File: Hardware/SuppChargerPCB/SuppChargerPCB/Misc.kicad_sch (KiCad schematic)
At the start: 11 parts, among them J3 Conn_01x02_Pin, J4 Conn_01x02_Pin, J5 Conn_01x02_Pin, J6 Conn_01x02_Pin, J7 Conn_01x02_Pin, J8 Conn_01x02_Pin

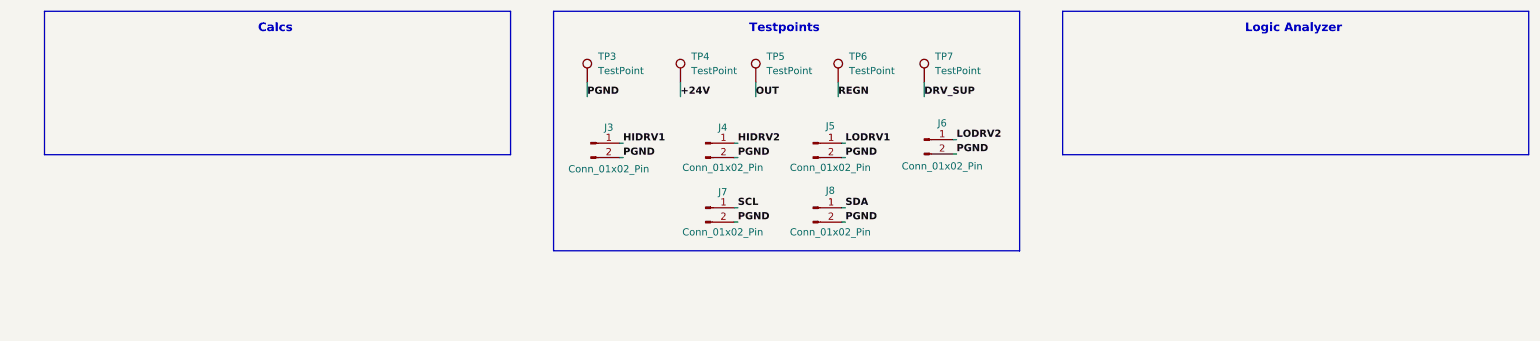
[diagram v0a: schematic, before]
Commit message: added calcs, logic analyzer
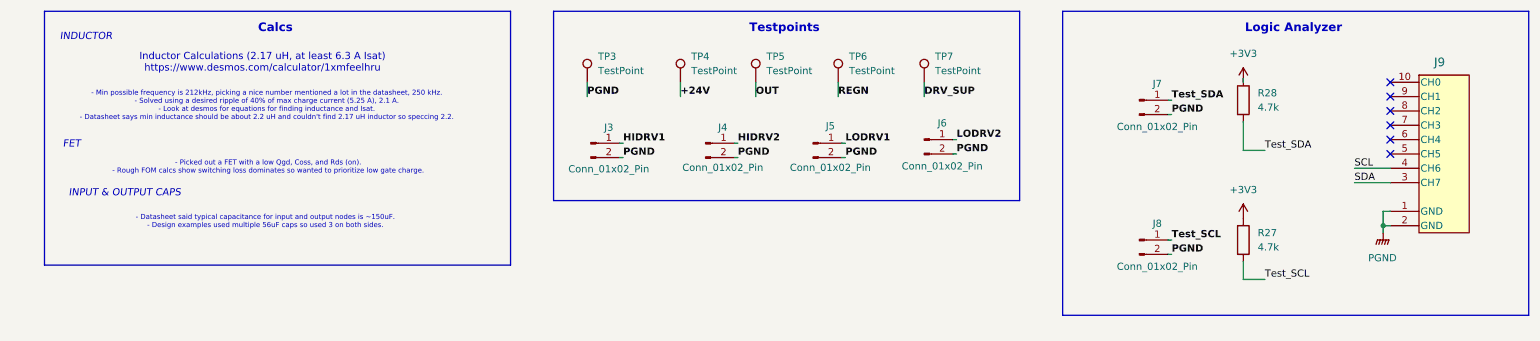
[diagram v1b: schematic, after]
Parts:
- added J9: SFH11-PBPC-D05-ST-BK, UTSVT_Connectors:CONN_SFH11-xxxC-D05-ST-XX_SUL, symbol utsvt_connectors:SFH11-PBPC-D05-ST-BK
- added R27, R28: 4.7k, symbol Device:R
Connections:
- net PGND: now also J9.1 (GND), J9.2 (GND)
- net SCL: now also J9.4 (CH6); no longer J7.1 (Pin_1)
- net SDA: now also J9.3 (CH7); no longer J8.1 (Pin_1)
- new net +3V3: R27.1, R28.1
- new net Test_SCL: J8.1 (Pin_1), R27.2
- new net Test_SDA: J7.1 (Pin_1), R28.2
- no-connect marks 0 -> 6
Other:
- note added: "- Datasheet said typical capacitance for input and output nodes is ~150uF. - Design examples used multiple 56uF caps so used 3 on both sides."
- note added: "- Min possible frequency is 212kHz, picking a nice number mentioned a lot in the datasheet, 250 kHz. - Solved using a desired ripple of 40% of max charge current (5.25 A), 2.1 A. - Look at desmos for equations for finding inductance and Isat. - Datasheet says min inductance should be about 2.2 uH and couldn't find 2.17 uH inductor so speccing 2.2."
- note added: "- Picked out a FET with a low Qgd, Coss, and Rds (on). - Rough FOM calcs show switching loss dominates so wanted to prioritize low gate charge."
- note added: "FET"
- note added: "INDUCTOR"
- note added: "INPUT & OUTPUT CAPS"
- note added: "Inductor Calculations (2.17 uH, at least 6.3 A Isat) https://www.desmos.com/calculator/1xmfeelhru"

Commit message: need to assign bulk cap
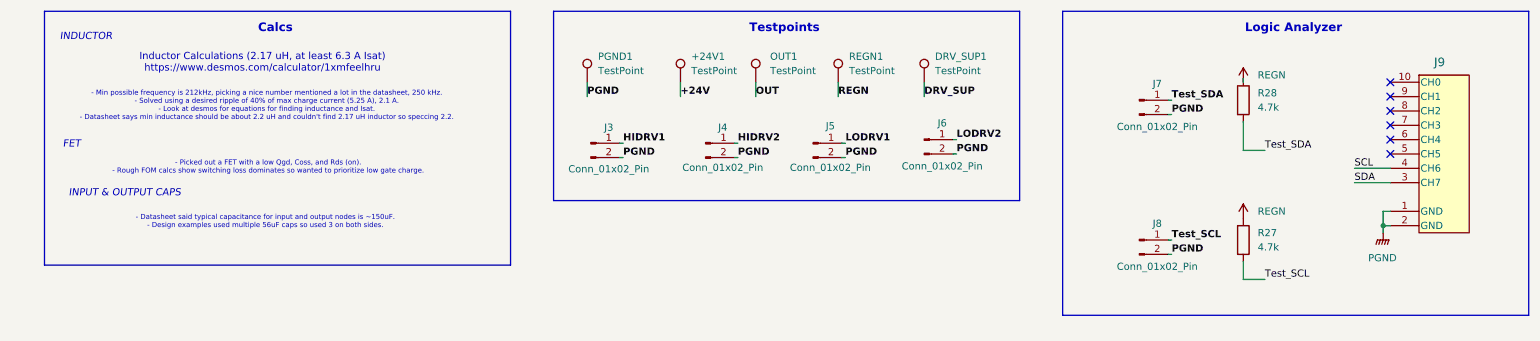
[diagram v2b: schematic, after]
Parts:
- +24V1: renamed from TP4; footprint (none) -> Connector_PinHeader_2.54mm:PinHeader_1x01_P2.54mm_Vertical
- DRV_SUP1: renamed from TP7; footprint (none) -> Connector_PinHeader_2.54mm:PinHeader_1x01_P2.54mm_Vertical
- J3, J4, J5, J6, J7, J8: footprint (none) -> Connector_PinHeader_2.54mm:PinHeader_1x02_P2.54mm_Vertical
- OUT1: renamed from TP5; footprint (none) -> Connector_PinHeader_2.54mm:PinHeader_1x01_P2.54mm_Vertical
- PGND1: renamed from TP3; footprint (none) -> Connector_PinHeader_2.54mm:PinHeader_1x01_P2.54mm_Vertical
- R27, R28: footprint (none) -> Resistor_SMD:R_0603_1608Metric; P/N (none) -> CRCW06034K70FKEA
- REGN1: renamed from TP6; footprint (none) -> Connector_PinHeader_2.54mm:PinHeader_1x01_P2.54mm_Vertical
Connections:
- net +3V3 is gone; now on net REGN: R27.1, R28.1
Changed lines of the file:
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@@
 			)
 		)
-		(property "Footprint" ""
+		(property "Footprint" "Resistor_SMD:R_0603_1608Metric"
 			(at 226.822 60.325 90)
 			(effects
@@
 			)
 		)
+		(property "P/N" "CRCW06034K70FKEA"
+			(at 228.6 60.325 0)
+			(effects
+				(font
+					(size 1.27 1.27)
+				)
+				(hide yes)
+			)
+		)
 		(pin "2"
 		)
@@
 		(dnp no)
 		(fields_autoplaced yes)
-		(property "Reference" "TP6"
+		(property "Reference" "REGN1"
 			(at 158.75 27.8129 0)
 			(effects
@@
 			)
 		)
-		(property "Footprint" ""
+		(property "Footprint" "Connector_PinHeader_2.54mm:PinHeader_1x01_P2.54mm_Vertical"
 			(at 161.925 32.385 0)
 			(effects
@@
 			(project "SuppChargerPCB"
 				(path "/ef3612d5-925d-4729-8ba2-cd35f149d39a/a4965329-5124-4c87-b9ed-641086cc0004"
-					(reference "TP6")
+					(reference "REGN1")
 					(unit 1)
 				)
@@
 			)
 		)
-		(property "Value" "+3V3"
-			(at 228.6 51.435 0)
-			(effects
-				(font
-					(size 1.27 1.27)
-				)
+		(property "Value" "REGN"
+			(at 231.14 55.2449 0)
+			(effects
+				(font
+					(size 1.27 1.27)
+				)
+				(justify left)
 			)
 		)
@@
 			)
 		)
-		(property "Footprint" ""
+		(property "Footprint" "Connector_PinHeader_2.54mm:PinHeader_1x02_P2.54mm_Vertical"
 			(at 210.185 60.325 0)
 			(effects
@@
 			)
 		)
-		(property "Footprint" ""
+		(property "Footprint" "Resistor_SMD:R_0603_1608Metric"
 			(at 226.822 35.56 90)
 			(effects
@@
 			)
 		)
+		(property "P/N" "CRCW06034K70FKEA"
+			(at 228.6 35.56 0)
+			(effects
+				(font
+					(size 1.27 1.27)
+				)
+				(hide yes)
+			)
+		)
 		(pin "2"
 		)
@@
 			)
 		)
-		(property "Footprint" ""
+		(property "Footprint" "Connector_PinHeader_2.54mm:PinHeader_1x02_P2.54mm_Vertical"
 			(at 133.35 43.18 0)
 			(effects
@@
 			)
 		)
-		(property "Footprint" ""
+		(property "Footprint" "Connector_PinHeader_2.54mm:PinHeader_1x02_P2.54mm_Vertical"
 			(at 172.085 42.545 0)
 			(effects
@@
 			)
 		)
-		(property "Footprint" ""
+		(property "Footprint" "Connector_PinHeader_2.54mm:PinHeader_1x02_P2.54mm_Vertical"
 			(at 113.03 43.18 0)
 			(effects
@@
 		(dnp no)
 		(fields_autoplaced yes)
-		(property "Reference" "TP5"
-			(at 144.145 27.8129 0)
+		(property "Reference" "OUT1"
+			(at 144.78 27.8129 0)
 			(effects
 				(font
@@
 		)
 		(property "Value" "TestPoint"
-			(at 144.145 30.3529 0)
-			(effects
-				(font
-					(size 1.27 1.27)
-				)
-				(justify left)
-			)
-		)
-		(property "Footprint" ""
+			(at 144.78 30.3529 0)
+			(effects
+				(font
+					(size 1.27 1.27)
+				)
+				(justify left)
+			)
+		)
+		(property "Footprint" "Connector_PinHeader_2.54mm:PinHeader_1x01_P2.54mm_Vertical"
 			(at 147.32 32.385 0)
 			(effects
@@
 			(project "SuppChargerPCB"
 				(path "/ef3612d5-925d-4729-8ba2-cd35f149d39a/a4965329-5124-4c87-b9ed-641086cc0004"
-					(reference "TP5")
+					(reference "OUT1")
 					(unit 1)
 				)
@@
 		(dnp no)
 		(fields_autoplaced yes)
-		(property "Reference" "TP4"
+		(property "Reference" "+24V1"
 			(at 130.81 27.8129 0)
 			(effects
@@
 			)
 		)
-		(property "Footprint" ""
+		(property "Footprint" "Connector_PinHeader_2.54mm:PinHeader_1x01_P2.54mm_Vertical"
 			(at 133.985 32.385 0)
 			(effects
@@
 			(project "SuppChargerPCB"
 				(path "/ef3612d5-925d-4729-8ba2-cd35f149d39a/a4965329-5124-4c87-b9ed-641086cc0004"
-					(reference "TP4")
+					(reference "+24V1")
 					(unit 1)
 				)
@@
 		(dnp no)
 		(fields_autoplaced yes)
-		(property "Reference" "TP7"
+		(property "Reference" "DRV_SUP1"
 			(at 173.99 27.8129 0)
 			(effects
@@
 			)
 		)
-		(property "Footprint" ""
+		(property "Footprint" "Connector_PinHeader_2.54mm:PinHeader_1x01_P2.54mm_Vertical"
 			(at 177.165 32.385 0)
 			(effects
@@
 			(project "SuppChargerPCB"
 				(path "/ef3612d5-925d-4729-8ba2-cd35f149d39a/a4965329-5124-4c87-b9ed-641086cc0004"
-					(reference "TP7")
+					(reference "DRV_SUP1")
 					(unit 1)
 				)
@@
 		(dnp no)
 		(fields_autoplaced yes)
-		(property "Reference" "TP3"
+		(property "Reference" "PGND1"
 			(at 114.3 27.8129 0)
 			(effects
@@
 			)
 		)
-		(property "Footprint" ""
+		(property "Footprint" "Connector_PinHeader_2.54mm:PinHeader_1x01_P2.54mm_Vertical"
 			(at 117.475 32.385 0)
 			(effects
@@
 			(project "SuppChargerPCB"
 				(path "/ef3612d5-925d-4729-8ba2-cd35f149d39a/a4965329-5124-4c87-b9ed-641086cc0004"
-					(reference "TP3")
+					(reference "PGND1")
 					(unit 1)
 				)
@@
 			)
 		)
-		(property "Footprint" ""
+		(property "Footprint" "Connector_PinHeader_2.54mm:PinHeader_1x02_P2.54mm_Vertical"
 			(at 152.4 43.18 0)
 			(effects
@@
 			)
 		)
-		(property "Footprint" ""
+		(property "Footprint" "Connector_PinHeader_2.54mm:PinHeader_1x02_P2.54mm_Vertical"
 			(at 210.185 35.56 0)
 			(effects
@@
 			)
 		)
-		(property "Value" "+3V3"
-			(at 228.6 27.305 0)
-			(effects
-				(font
-					(size 1.27 1.27)
-				)
-			)
-		)
+		(property "Value" "REGN"
+			(at 231.14 31.1149 0)
+			(effects
+				(font
+					(size 1.27 1.27)
+				)
+				(justify left)
+			)
+		)

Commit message: abused pwr flags
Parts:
- removed DRV_SUP1, REGN1: TestPoint, Connector_PinHeader_2.54mm:PinHeader_1x01_P2.54mm_Vertical, symbol Connector:TestPoint
- removed J7, J8: Conn_01x02_Pin, Connector_PinHeader_2.54mm:PinHeader_1x02_P2.54mm_Vertical, symbol Connector:Conn_01x02_Pin
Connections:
- net SCL is gone; now on net Test_SCL: J9.4 (CH6)
- net SDA is gone; now on net Test_SDA: J9.3 (CH7)
- net PGND: no longer J9.1 (GND), J9.2 (GND)
- net Test_SCL: now also R28.2; no longer R27.2
- net Test_SDA: now also R27.2; no longer R28.2
- net REGN renamed +3V3
- new net GND_TEST: J9.1 (GND)
- no-connect marks 6 -> 7
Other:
- note added: "- Datasheet said typical capacitance for input and output nodes is ~150uF. - Design examples used multiple 56uF caps so used 3 on both sides. - Don't need much ripple current capacity"
- note removed: "- Datasheet said typical capacitance for input and output nodes is ~150uF. - Design examples used multiple 56uF caps so used 3 on both sides."
- moved on the sheet: +24V1, J9, OUT1, PGND1, R27, R28

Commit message: pre sheet reorg
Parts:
- added ACOV1, ACUV1: TestPoint, Connector_PinHeader_2.54mm:PinHeader_1x01_P2.54mm_Vertical, symbol Connector:TestPoint
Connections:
- net GND_TEST is gone; now on net PGND: J9.1 (GND)
- net PGND: now also ACOV1.1, ACUV1.1
- net Test_SCL: no longer names the net of J9.4 (CH6), R28.2
- net Test_SDA renamed SDA
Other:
- note added: "Inductor Calculations (2.17 uH, at least 6.3 A Isat)"
- note added: "add test points that aren't immediately able to b measured"
- note removed: "Inductor Calculations (2.17 uH, at least 6.3 A Isat) https://www.desmos.com/calculator/1xmfeelhru"
